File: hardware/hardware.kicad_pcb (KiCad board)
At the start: 2 copper layers, 83 x 54.5 mm, 18 parts, among them J1 Screw_Terminal_01x02, J2 Screw_Terminal_01x02, J3 Screw_Terminal_01x02, K1 RM85-2011-35-1005, K2 RM85-2011-35-1005, Q1 BC337, Q2 BC337, U1 XIAO-ESP32-C6, U2 DS18B20

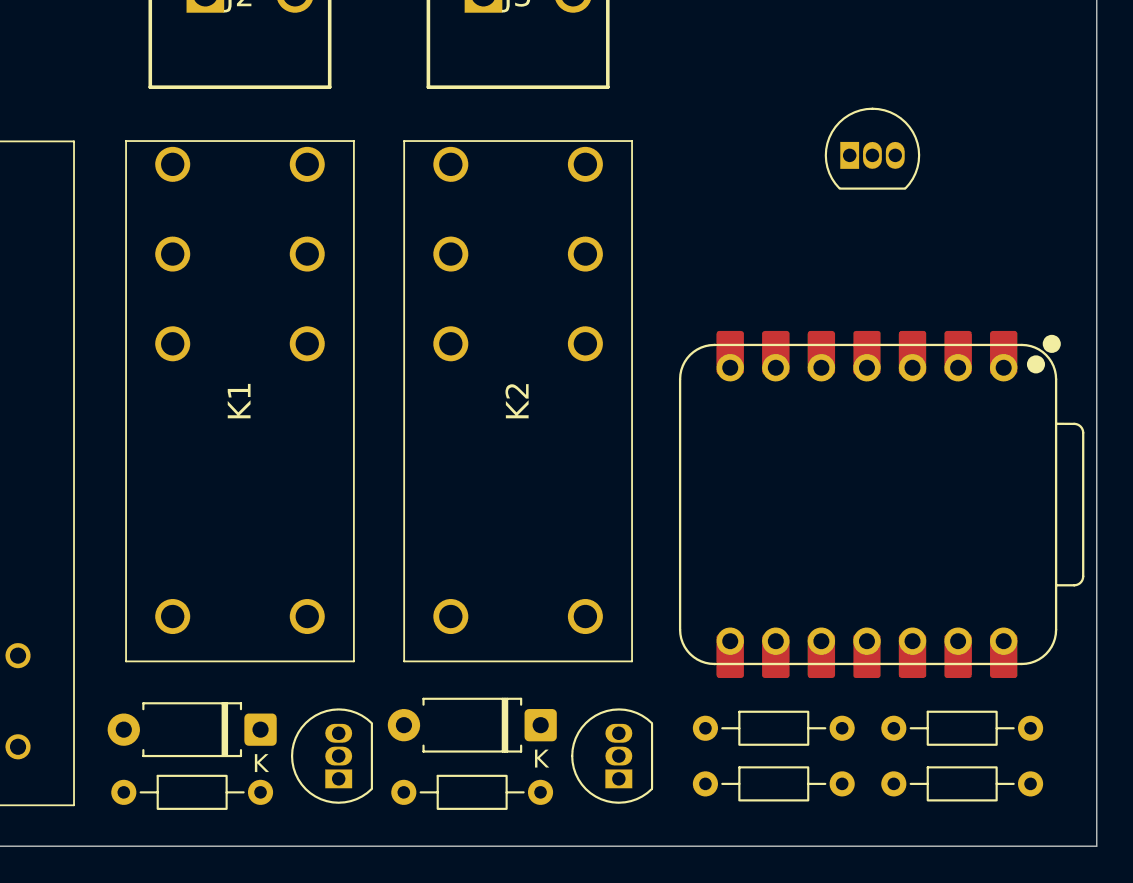
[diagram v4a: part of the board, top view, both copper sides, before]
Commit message: Removed DS18B20 temp sensor
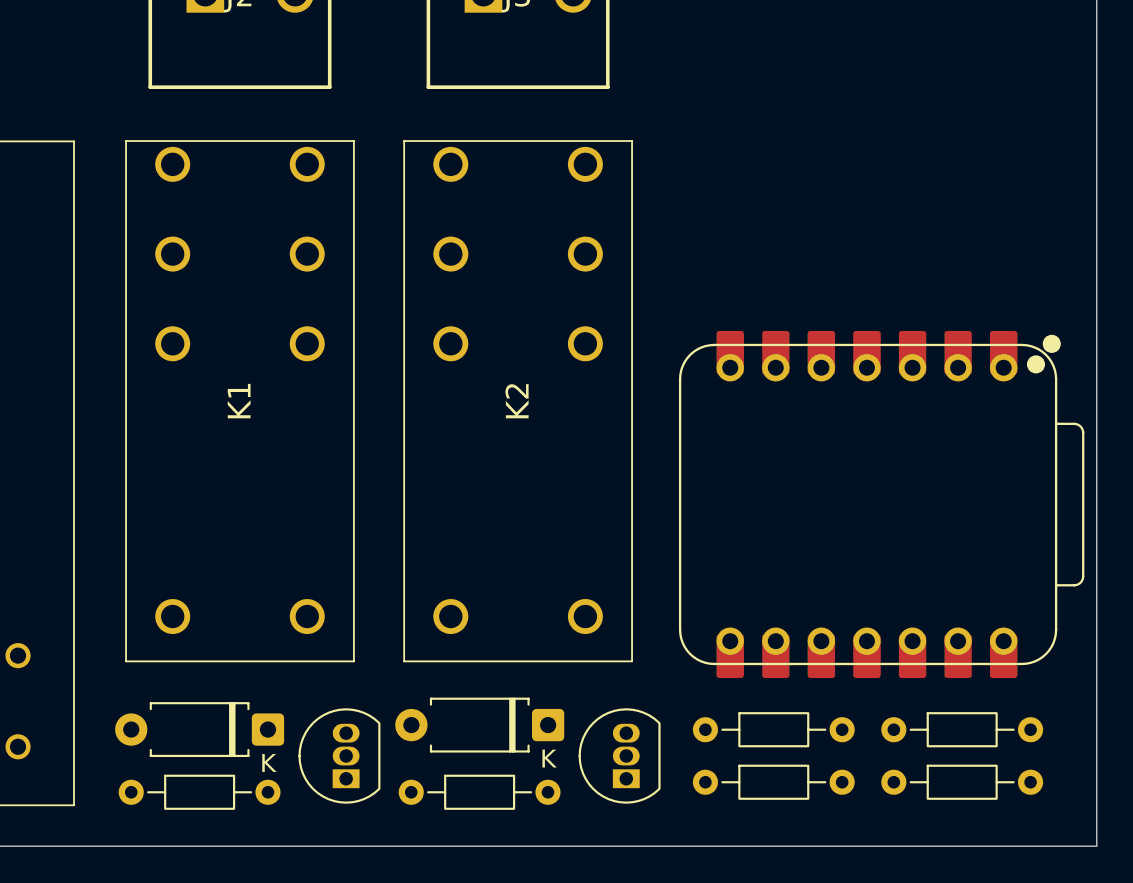
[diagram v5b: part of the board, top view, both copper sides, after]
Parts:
- removed U2: DS18B20, Package_TO_SOT_THT:TO-92_Inline
- moved R5 3.02 mm to (76.2, 63.0)
- moved R6 3.02 mm to (86.7, 63.0)
- moved R2 3.01 mm to (86.7, 65.9)
- moved R4 3.01 mm to (76.2, 65.9)
- moved D2 0.42 mm to (67.4, 62.8)
- moved Q2 0.42 mm to (71.8, 65.7)
- moved D1 0.42 mm to (51.8, 63.0)
- moved Q1 0.42 mm to (56.2, 65.7)
- moved R1 0.42 mm to (44.2, 66.5)
- moved R3 0.42 mm to (59.8, 66.5)
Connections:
- U1 pad 10: RELAY_A_CTRL -> RELAY_B_CTRL
- U1 pad 3: TEMP_SENSOR_DATA -> unconnected-(U1-GPIO2/A2/D2-Pad3)
- U1 pad 9: RELAY_B_CTRL -> RELAY_A_CTRL
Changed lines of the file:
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@@
 	(net 27 "unconnected-(U1-GPIO16{slash}D6{slash}TX-Pad7)")
 	(net 28 "unconnected-(U1-GPIO23{slash}D5{slash}SCL-Pad6)")
-	(net 29 "TEMP_SENSOR_DATA")
-	(net 30 "unconnected-(U1-GPIO0{slash}A0{slash}D0-Pad1)")
-	(net 31 "unconnected-(U1-GPIO1{slash}A1{slash}D1-Pad2)")
+	(net 29 "unconnected-(U1-GPIO0{slash}A0{slash}D0-Pad1)")
+	(net 30 "unconnected-(U1-GPIO1{slash}A1{slash}D1-Pad2)")
+	(net 31 "unconnected-(U1-GPIO2{slash}A2{slash}D2-Pad3)")
 	(footprint "Degson Electronics:DG1285002P14"
 		(locked yes)
@@
 			(layers "F.Cu" "F.Mask")
 			(roundrect_rratio 0.1)
-			(net 30 "unconnected-(U1-GPIO0{slash}A0{slash}D0-Pad1)")
+			(net 29 "unconnected-(U1-GPIO0{slash}A0{slash}D0-Pad1)")
 			(pinfunction "GPIO0/A0/D0")
 			(pintype "passive")
@@
 			(layers "*.Cu" "*.Mask")
 			(remove_unused_layers no)
-			(net 30 "unconnected-(U1-GPIO0{slash}A0{slash}D0-Pad1)")
+			(net 29 "unconnected-(U1-GPIO0{slash}A0{slash}D0-Pad1)")
 			(pinfunction "GPIO0/A0/D0")
 			(pintype "passive")
@@
 			(layers "F.Cu" "F.Mask")
 			(roundrect_rratio 0.1)
-			(net 31 "unconnected-(U1-GPIO1{slash}A1{slash}D1-Pad2)")
+			(net 30 "unconnected-(U1-GPIO1{slash}A1{slash}D1-Pad2)")
 			(pinfunction "GPIO1/A1/D1")
 			(pintype "passive")
@@
 			(layers "*.Cu" "*.Mask")
 			(remove_unused_layers no)
-			(net 31 "unconnected-(U1-GPIO1{slash}A1{slash}D1-Pad2)")
+			(net 30 "unconnected-(U1-GPIO1{slash}A1{slash}D1-Pad2)")
 			(pinfunction "GPIO1/A1/D1")
 			(pintype "passive")
@@
 			(layers "F.Cu" "F.Mask")
 			(roundrect_rratio 0.1)
-			(net 29 "TEMP_SENSOR_DATA")
+			(net 31 "unconnected-(U1-GPIO2{slash}A2{slash}D2-Pad3)")
 			(pinfunction "GPIO2/A2/D2")
 			(pintype "passive")
@@
 			(layers "*.Cu" "*.Mask")
 			(remove_unused_layers no)
-			(net 29 "TEMP_SENSOR_DATA")
+			(net 31 "unconnected-(U1-GPIO2{slash}A2{slash}D2-Pad3)")
 			(pinfunction "GPIO2/A2/D2")
 			(pintype "passive")
@@
 			(layers "*.Cu" "*.Mask")
 			(remove_unused_layers no)
-			(net 22 "RELAY_B_CTRL")
+			(net 21 "RELAY_A_CTRL")
 			(pinfunction "GPIO19/D8/SCK")
 			(pintype "passive")
@@
 			(layers "F.Cu" "F.Mask")
 			(roundrect_rratio 0.1)
-			(net 22 "RELAY_B_CTRL")
+			(net 21 "RELAY_A_CTRL")
 			(pinfunction "GPIO19/D8/SCK")
 			(pintype "passive")
@@
 			(layers "*.Cu" "*.Mask")
 			(remove_unused_layers no)
-			(net 21 "RELAY_A_CTRL")
+			(net 22 "RELAY_B_CTRL")
 			(pinfunction "GPIO20/D9/MISO")
 			(pintype "passive")
@@
 			(layers "F.Cu" "F.Mask")
 			(roundrect_rratio 0.1)
-			(net 21 "RELAY_A_CTRL")
+			(net 22 "RELAY_B_CTRL")
 			(pinfunction "GPIO20/D9/MISO")
 			(pintype "passive")
@@
 		(locked yes)
 		(layer "F.Cu")
-		(at 51.395 63.005 180)
+		(at 51.81 63 180)
 		(descr "Diode, A-405 series, Axial, Horizontal, pin pitch=7.62mm, length*diameter=5.2*2.7mm^2, http://www.diodes.com/_files/packages/A-405.pdf")
 		(tags "Diode A-405 series Axial Horizontal pin pitch 7.62mm  length 5.2mm diameter 2.7mm")
@@
 		(locked yes)
 		(layer "F.Cu")
-		(at 59.38 66.5)
+		(at 59.795 66.495)
 		(descr "Resistor, Axial_DIN0204 series, Axial, Horizontal, pin pitch=7.62mm, 0.167W, length*diameter=3.6*1.6mm^2, http://cdn-reichelt.de/documents/datenblatt/B400/1_4W%23YAG.pdf")
 		(tags "Resistor Axial_DIN0204 series Axial Horizontal pin pitch 7.62mm 0.167W length 3.6mm diameter 1.6mm")
@@
 		(locked yes)
 		(layer "F.Cu")
-		(at 67.008333 62.755 180)
+		(at 67.423333 62.75 180)
 		(descr "Diode, A-405 series, Axial, Horizontal, pin pitch=7.62mm, length*diameter=5.2*2.7mm^2, http://www.diodes.com/_files/packages/A-405.pdf")
 		(tags "Diode A-405 series Axial Horizontal pin pitch 7.62mm  length 5.2mm diameter 2.7mm")
@@
 		(locked yes)
 		(layer "F.Cu")
-		(at 71.365 65.7475 90)
+		(at 71.78 65.7425 90)
 		(descr "TO-92 leads in-line, narrow, oval pads, drill 0.75mm (see NXP sot054_po.pdf)")
 		(tags "to-92 sc-43 sc-43a sot54 PA33 transistor")
@@
 		(locked yes)
 		(layer "F.Cu")
-		(at 76.19 66.0275)
+		(at 76.19 63.00875)
 		(descr "Resistor, Axial_DIN0204 series, Axial, Horizontal, pin pitch=7.62mm, 0.167W, length*diameter=3.6*1.6mm^2, http://cdn-reichelt.de/documents/datenblatt/B400/1_4W%23YAG.pdf")
 		(tags "Resistor Axial_DIN0204 series Axial Horizontal pin pitch 7.62mm 0.167W length 3.6mm diameter 1.6mm")
@@
 		(locked yes)
 		(layer "F.Cu")
-		(at 76.19 62.9275)
+		(at 76.19 65.93625)
 		(descr "Resistor, Axial_DIN0204 series, Axial, Horizontal, pin pitch=7.62mm, 0.167W, length*diameter=3.6*1.6mm^2, http://cdn-reichelt.de/documents/datenblatt/B400/1_4W%23YAG.pdf")
 		(tags "Resistor Axial_DIN0204 series Axial Horizontal pin pitch 7.62mm 0.167W length 3.6mm diameter 1.6mm")
@@
 		(locked yes)
 		(layer "F.Cu")
-		(at 86.69 66.0275)
+		(at 86.69 63.00875)
 		(descr "Resistor, Axial_DIN0204 series, Axial, Horizontal, pin pitch=7.62mm, 0.167W, length*diameter=3.6*1.6mm^2, http://cdn-reichelt.de/documents/datenblatt/B400/1_4W%23YAG.pdf")
 		(tags "Resistor Axial_DIN0204 series Axial Horizontal pin pitch 7.62mm 0.167W length 3.6mm diameter 1.6mm")
@@
 		(locked yes)
 		(layer "F.Cu")
-		(at 86.69 62.9275)
+		(at 86.69 65.93625)
 		(descr "Resistor, Axial_DIN0204 series, Axial, Horizontal, pin pitch=7.62mm, 0.167W, length*diameter=3.6*1.6mm^2, http://cdn-reichelt.de/documents/datenblatt/B400/1_4W%23YAG.pdf")
 		(tags "Resistor Axial_DIN0204 series Axial Horizontal pin pitch 7.62mm 0.167W length 3.6mm diameter 1.6mm")
@@
 		(locked yes)
 		(layer "F.Cu")
-		(at 43.775 66.5)
+		(at 44.19 66.495)
 		(descr "Resistor, Axial_DIN0204 series, Axial, Horizontal, pin pitch=7.62mm, 0.167W, length*diameter=3.6*1.6mm^2, http://cdn-reichelt.de/documents/datenblatt/B400/1_4W%23YAG.pdf")
 		(tags "Resistor Axial_DIN0204 series Axial Horizontal pin pitch 7.62mm 0.167W length 3.6mm diameter 1.6mm")
@@
 		(locked yes)
 		(layer "F.Cu")
-		(at 55.751667 65.7475 90)
+		(at 56.166667 65.7425 90)
 		(descr "TO-92 leads in-line, narrow, oval pads, drill 0.75mm (see NXP sot054_po.pdf)")
 		(tags "to-92 sc-43 sc-43a sot54 PA33 transistor")
@@
 		)
 		(embedded_fonts no)
-		(model "${KICAD9_3DMODEL_DIR}/Package_TO_SOT_THT.3dshapes/TO-92_Inline.step"
-			(offset
-				(xyz 0 0 0)
-			)
-			(scale
-				(xyz 1 1 1)
-			)
-			(rotate
-				(xyz 0 0 0)
-			)
-		)
-	)
-	(footprint "Package_TO_SOT_THT:TO-92_Inline"
-		(layer "F.Cu")
-		(at 84.23 31)
-		(descr "TO-92 leads in-line, narrow, oval pads, drill 0.75mm (see NXP sot054_po.pdf)")
-		(tags "to-92 sc-43 sc-43a sot54 PA33 transistor")
-		(property "Reference" "U2"
-			(at 1.27 -3.56 0)
-			(layer "F.SilkS")
-			(hide yes)
-			(effects
-				(font
-					(size 1 1)
-					(thickness 0.15)
-				)
-			)
-		)
-		(property "Value" "DS18B20"
-			(at 1.27 2.79 0)
-			(layer "F.Fab")
-			(hide yes)
-			(effects
-				(font
-					(size 1 1)
-					(thickness 0.15)
-				)
-			)
-		)
-		(property "Datasheet" "http://datasheets.maximintegrated.com/en/ds/DS18B20.pdf"
-			(at 0 0 0)
-			(unlocked yes)
-			(layer "F.Fab")
-			(hide yes)
-			(effects
-				(font
-					(size 1.27 1.27)
-					(thickness 0.15)
-				)
-			)
-		)
-		(property "Description" "Programmable Resolution 1-Wire Digital Thermometer TO-92"
-			(at 0 0 0)
-			(unlocked yes)
-			(layer "F.Fab")
-			(hide yes)
-			(effects
-				(font
-					(size 1.27 1.27)
-					(thickness 0.15)
-				)
-			)
-		)
-		(property ki_fp_filters "TO*92*")
-		(sheetname "/")
-		(sheetfile "hardware.kicad_sch")
-		(attr through_hole)
-		(fp_line
-			(start -0.53 1.85)
-			(end 3.07 1.85)
-			(stroke
-				(width 0.12)
-				(type solid)
-			)
-			(layer "F.SilkS")
-		)
-		(fp_arc
-			(start -0.568478 1.838478)
-			(mid -1.132087 -0.994977)
-			(end 1.27 -2.6)
-			(stroke
-				(width 0.12)
-				(type solid)
-			)
-			(layer "F.SilkS")
-		)
-		(fp_arc
-			(start 1.27 -2.6)
-			(mid 3.672087 -0.994977)
-			(end 3.108478 1.838478)
-			(stroke
-				(width 0.12)
-				(type solid)
-			)
-			(layer "F.SilkS")
-		)
-		(fp_line
-			(start -1.46 -2.73)
-			(end -1.46 2.01)
-			(stroke
-				(width 0.05)
-				(type solid)
-			)
-			(layer "F.CrtYd")
-		)
-		(fp_line
-			(start -1.46 -2.73)
-			(end 4 -2.73)
-			(stroke
-				(width 0.05)
-				(type solid)
-			)
-			(layer "F.CrtYd")
-		)
-		(fp_line
-			(start 4 2.01)
-			(end -1.46 2.01)
-			(stroke
-				(width 0.05)
-				(type solid)
-			)
-			(layer "F.CrtYd")
-		)
-		(fp_line
-			(start 4 2.01)
-			(end 4 -2.73)
-			(stroke
-				(width 0.05)
-				(type solid)
-			)
-			(layer "F.CrtYd")
-		)
-		(fp_line
-			(start -0.5 1.75)
-			(end 3 1.75)
-			(stroke
-				(width 0.1)
-				(type solid)
-			)
-			(layer "F.Fab")
-		)
-		(fp_arc
-			(start -0.483625 1.753625)
-			(mid -1.021221 -0.949055)
-			(end 1.27 -2.48)
-			(stroke
-				(width 0.1)
-				(type solid)
-			)
-			(layer "F.Fab")
-		)
-		(fp_arc
-			(start 1.27 -2.48)
-			(mid 3.561221 -0.949055)
-			(end 3.023625 1.753625)
-			(stroke
-				(width 0.1)
-				(type solid)
-			)
-			(layer "F.Fab")
-		)
-		(fp_text user "${REFERENCE}"
-			(at 1.27 0 0)
-			(layer "F.Fab")
-			(effects
-				(font
-					(size 1 1)
-					(thickness 0.15)
-				)
-			)
-		)
-		(pad "1" thru_hole rect
-			(at 0 0)
-			(size 1.05 1.5)
-			(drill 0.75)
-			(layers "*.Cu" "*.Mask")
-			(remove_unused_layers no)
-			(net 16 "GND")
-			(pinfunction "GND")
-			(pintype "power_in")
-		)
-		(pad "2" thru_hole oval
-			(at 1.27 0)
-			(size 1.05 1.5)
-			(drill 0.75)
-			(layers "*.Cu" "*.Mask")
-			(remove_unused_layers no)
-			(net 29 "TEMP_SENSOR_DATA")
-			(pinfunction "DQ")
-			(pintype "bidirectional")
-		)
-		(pad "3" thru_hole oval
-			(at 2.54 0)
-			(size 1.05 1.5)
-			(drill 0.75)
-			(layers "*.Cu" "*.Mask")
-			(remove_unused_layers no)
-			(net 4 "+3V3")
-			(pinfunction "V_{DD}")
-			(pintype "power_in")
-		)
-		(embedded_fonts no)

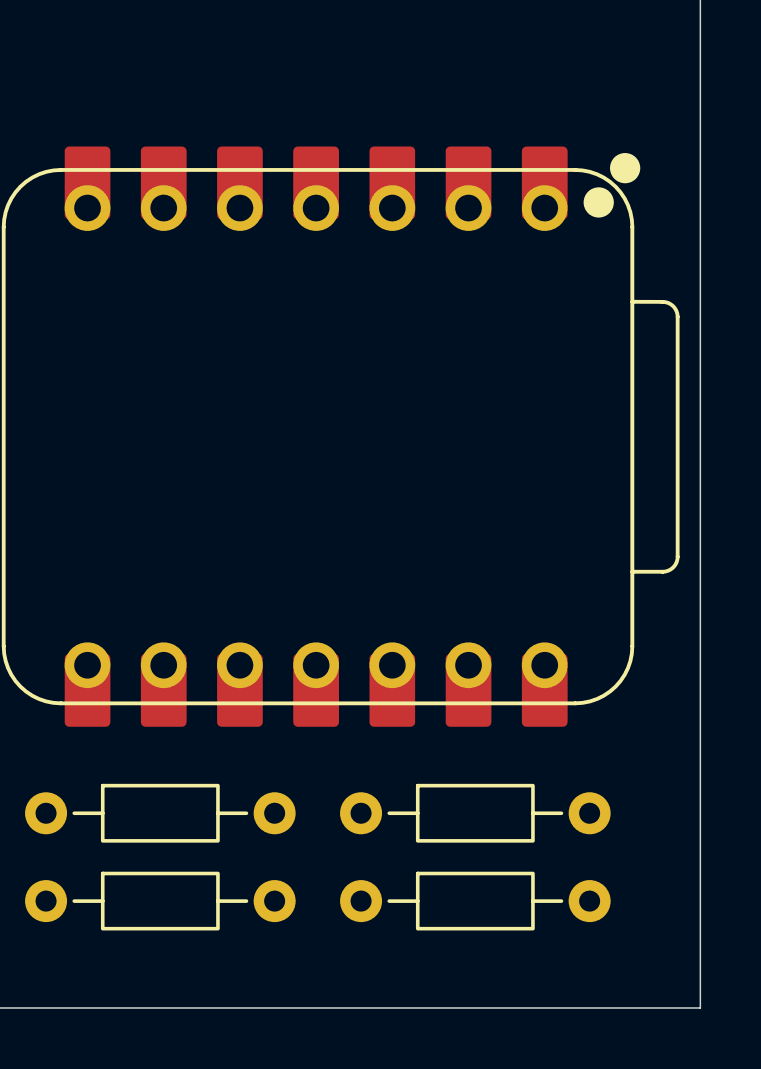
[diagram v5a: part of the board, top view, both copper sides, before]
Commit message: Started working on PCB traces
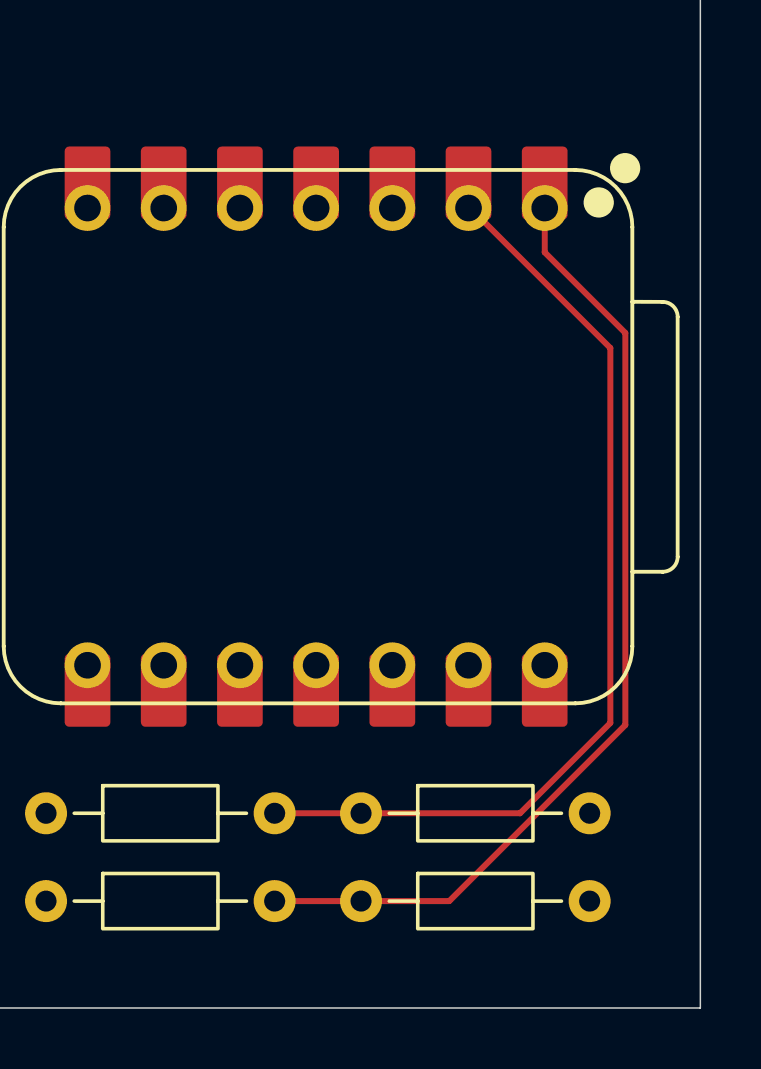
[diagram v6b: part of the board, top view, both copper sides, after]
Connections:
- U1 pad 1: unconnected-(U1-GPIO0/A0/D0-Pad1) -> RELAY_A_CTRL
- U1 pad 10: RELAY_B_CTRL -> unconnected-(U1-GPIO20/D9/MISO-Pad10)
- U1 pad 2: unconnected-(U1-GPIO1/A1/D1-Pad2) -> RELAY_B_CTRL
- U1 pad 9: RELAY_A_CTRL -> unconnected-(U1-GPIO19/D8/SCK-Pad9)
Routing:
- net RELAY_A_CTRL: track 0.00 -> 32.5 mm
- net RELAY_B_CTRL: track 0.00 -> 32.4 mm
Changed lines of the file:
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@@
 	(net 27 "unconnected-(U1-GPIO16{slash}D6{slash}TX-Pad7)")
 	(net 28 "unconnected-(U1-GPIO23{slash}D5{slash}SCL-Pad6)")
-	(net 29 "unconnected-(U1-GPIO0{slash}A0{slash}D0-Pad1)")
-	(net 30 "unconnected-(U1-GPIO1{slash}A1{slash}D1-Pad2)")
-	(net 31 "unconnected-(U1-GPIO2{slash}A2{slash}D2-Pad3)")
+	(net 29 "unconnected-(U1-GPIO2{slash}A2{slash}D2-Pad3)")
+	(net 30 "unconnected-(U1-GPIO20{slash}D9{slash}MISO-Pad10)")
+	(net 31 "unconnected-(U1-GPIO19{slash}D8{slash}SCK-Pad9)")
 	(footprint "Degson Electronics:DG1285002P14"
 		(locked yes)
@@
 			(layers "F.Cu" "F.Mask")
 			(roundrect_rratio 0.1)
-			(net 29 "unconnected-(U1-GPIO0{slash}A0{slash}D0-Pad1)")
+			(net 21 "RELAY_A_CTRL")
 			(pinfunction "GPIO0/A0/D0")
 			(pintype "passive")
@@
 			(layers "*.Cu" "*.Mask")
 			(remove_unused_layers no)
-			(net 29 "unconnected-(U1-GPIO0{slash}A0{slash}D0-Pad1)")
+			(net 21 "RELAY_A_CTRL")
 			(pinfunction "GPIO0/A0/D0")
 			(pintype "passive")
@@
 			(layers "F.Cu" "F.Mask")
 			(roundrect_rratio 0.1)
-			(net 30 "unconnected-(U1-GPIO1{slash}A1{slash}D1-Pad2)")
+			(net 22 "RELAY_B_CTRL")
 			(pinfunction "GPIO1/A1/D1")
 			(pintype "passive")
@@
 			(layers "*.Cu" "*.Mask")
 			(remove_unused_layers no)
-			(net 30 "unconnected-(U1-GPIO1{slash}A1{slash}D1-Pad2)")
+			(net 22 "RELAY_B_CTRL")
 			(pinfunction "GPIO1/A1/D1")
 			(pintype "passive")
@@
 			(layers "F.Cu" "F.Mask")
 			(roundrect_rratio 0.1)
-			(net 31 "unconnected-(U1-GPIO2{slash}A2{slash}D2-Pad3)")
+			(net 29 "unconnected-(U1-GPIO2{slash}A2{slash}D2-Pad3)")
 			(pinfunction "GPIO2/A2/D2")
 			(pintype "passive")
@@
 			(layers "*.Cu" "*.Mask")
 			(remove_unused_layers no)
-			(net 31 "unconnected-(U1-GPIO2{slash}A2{slash}D2-Pad3)")
+			(net 29 "unconnected-(U1-GPIO2{slash}A2{slash}D2-Pad3)")
 			(pinfunction "GPIO2/A2/D2")
 			(pintype "passive")
@@
 			(layers "*.Cu" "*.Mask")
 			(remove_unused_layers no)
-			(net 21 "RELAY_A_CTRL")
+			(net 31 "unconnected-(U1-GPIO19{slash}D8{slash}SCK-Pad9)")
 			(pinfunction "GPIO19/D8/SCK")
 			(pintype "passive")
@@
 			(layers "F.Cu" "F.Mask")
 			(roundrect_rratio 0.1)
-			(net 21 "RELAY_A_CTRL")
+			(net 31 "unconnected-(U1-GPIO19{slash}D8{slash}SCK-Pad9)")
 			(pinfunction "GPIO19/D8/SCK")
 			(pintype "passive")
@@
 			(layers "*.Cu" "*.Mask")
 			(remove_unused_layers no)
-			(net 22 "RELAY_B_CTRL")
+			(net 30 "unconnected-(U1-GPIO20{slash}D9{slash}MISO-Pad10)")
 			(pinfunction "GPIO20/D9/MISO")
 			(pintype "passive")
@@
 			(layers "F.Cu" "F.Mask")
 			(roundrect_rratio 0.1)
-			(net 22 "RELAY_B_CTRL")
+			(net 30 "unconnected-(U1-GPIO20{slash}D9{slash}MISO-Pad10)")
 			(pinfunction "GPIO20/D9/MISO")
 			(pintype "passive")
@@
 		(layer "Edge.Cuts")
 	)
+	(segment
+		(start 89.63085 65.93625)
+		(end 86.69 65.93625)
+		(width 0.2)
+		(layer "F.Cu")
+		(net 21)
+	)
+	(segment
+		(start 95.5 47)
+		(end 95.5 60.0671)
+		(width 0.2)
+		(layer "F.Cu")
+		(net 21)
+	)
+	(segment
+		(start 83.81 65.93625)
+		(end 86.69 65.93625)
+		(width 0.2)
+		(layer "F.Cu")
+		(net 21)
+	)
+	(segment
+		(start 92.8125 42.835)
+		(end 92.8125 44.3125)
+		(width 0.2)
+		(layer "F.Cu")
+		(net 21)
+	)
+	(segment
+		(start 92.8125 44.3125)
+		(end 95.5 47)
+		(width 0.2)
+		(layer "F.Cu")
+		(net 21)
+	)
+	(segment
+		(start 95.5 60.0671)
+		(end 89.63085 65.93625)
+		(width 0.2)
+		(layer "F.Cu")
+		(net 21)
+	)
+	(segment
+		(start 90.2725 42.7725)
+		(end 90.2725 42)
+		(width 0.2)
+		(layer "F.Cu")
+		(net 22)
+	)
+	(segment
+		(start 86.69 63.00875)
+		(end 91.99125 63.00875)
+		(width 0.2)
+		(layer "F.Cu")
+		(net 22)
+	)
+	(segment
+		(start 91.99125 63.00875)
+		(end 95 60)
+		(width 0.2)
+		(layer "F.Cu")
+		(net 22)
+	)
+	(segment
+		(start 95 47.5)
+		(end 90.2725 42.7725)
+		(width 0.2)
+		(layer "F.Cu")
+		(net 22)
+	)
+	(segment
+		(start 83.81 63.00875)
+		(end 86.69 63.00875)
+		(width 0.2)
+		(layer "F.Cu")
+		(net 22)
+	)
+	(segment
+		(start 95 60)
+		(end 95 47.5)
+		(width 0.2)
+		(layer "F.Cu")
+		(net 22)
+	)
 	(group ""
